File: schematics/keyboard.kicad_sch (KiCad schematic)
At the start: 32 parts, among them J2 Mini-DIN-6, Q1 2N7000, Q2 2N7000, Q3 2N7000, Q4 2N7000, Q5 2N7000, U18 74HC14, U19 74HC04, U21 ATF22V10C-7, U22 74HC280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

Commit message: done wiring
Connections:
- net D5: now also U21.17 (D5), U21.8 (D5IN)
- net D6: now also U21.16 (D6)
- net D7: now also U21.15 (D7)
- net GND: now also U19.5; no longer U19.3
- net at U22.2 (I7), U23.5 (G), U26.2 (QC)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: no longer U21.15 (D7)
- net at U22.1 (I6), U23.6 (H), U26.3 (QD)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: no longer U21.16 (D6)
- net at U22.13 (I5), U25.11 (A), U26.4 (QE)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: no longer U21.17 (D5), U21.8 (D5IN)
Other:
- moved on the sheet: Q5

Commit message: clock improvements
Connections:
- net ϕ0 renamed ϕ0.0
- net ϕ2 renamed ϕ2.0
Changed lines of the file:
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@@
 		)
 	)
-	(global_label "ϕ2"
+	(global_label "ϕ2.0"
 		(shape input)
 		(at 66.04 40.64 180)
@@
 		)
 		(property "Intersheetrefs" "${INTERSHEET_REFS}"
-			(at 60.5148 40.64 0)
+			(at 58.7005 40.64 0)
 			(hide yes)
 			(show_name no)
@@
 		)
 	)
-	(global_label "ϕ0"
+	(global_label "ϕ0.0"
 		(shape input)
 		(at 66.04 38.1 180)
@@
 		)
 		(property "Intersheetrefs" "${INTERSHEET_REFS}"
-			(at 60.5148 38.1 0)
+			(at 58.7005 38.1 0)
 			(hide yes)
 			(show_name no)

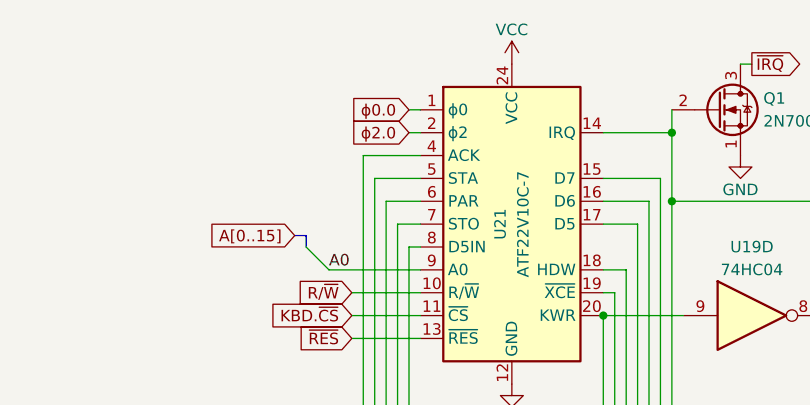
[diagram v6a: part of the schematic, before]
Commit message: ditched phi0, dropped to 6MHz
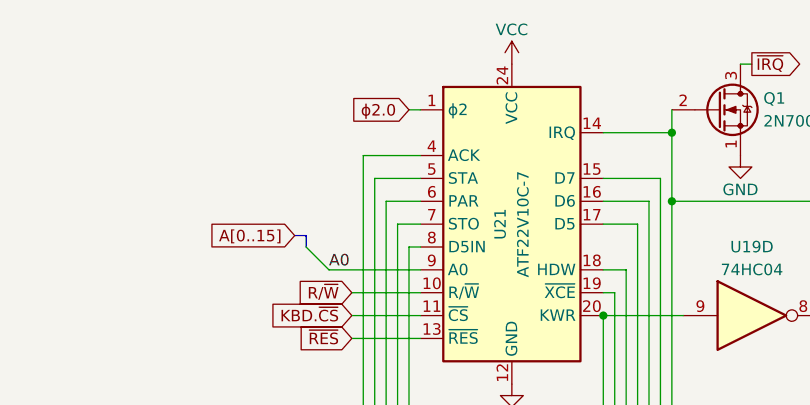
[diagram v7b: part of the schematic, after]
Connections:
- net ϕ0.0 is gone; now on net ϕ2.0: U21.1 (ϕ2)
- net ϕ2.0: no longer U21.2 (ϕ2)
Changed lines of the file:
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@@
-	(wire
-		(pts
-			(xy 66.04 40.64) (xy 67.31 40.64)
-		)
-		(stroke
-			(width 0)
-			(type default)
-		)
-	)
 	(wire
 		(pts
@@
 		)
 	)
-	(global_label "ϕ2.0"
-		(shape input)
-		(at 66.04 40.64 180)
-		(fields_autoplaced yes)
-		(effects
-			(font
-				(size 1.27 1.27)
-			)
-			(justify right)
-		)
-		(property "Intersheetrefs" "${INTERSHEET_REFS}"
-			(at 58.7005 40.64 0)
-			(hide yes)
-			(show_name no)
-			(do_not_autoplace no)
-			(effects
-				(font
-					(size 1.27 1.27)
-				)
-				(justify right)
-			)
-		)
-	)
 	(global_label "KBD.~{CS}"
 		(shape input)
@@
 		)
 	)
-	(global_label "ϕ0.0"
+	(global_label "ϕ2.0"
 		(shape input)
 		(at 66.04 38.1 180)

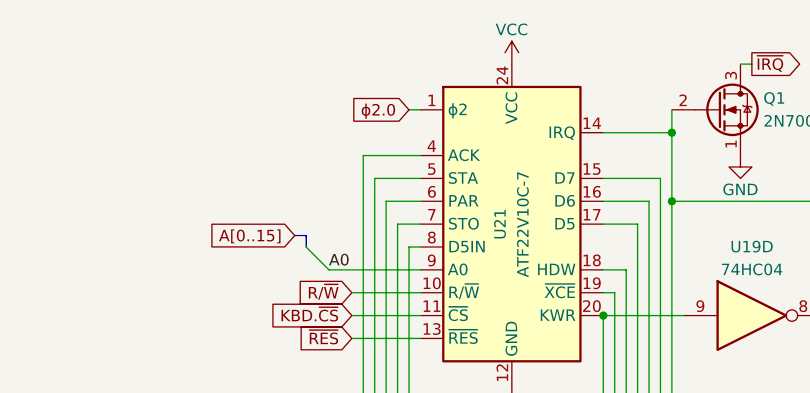
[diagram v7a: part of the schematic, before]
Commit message: keyboard input works
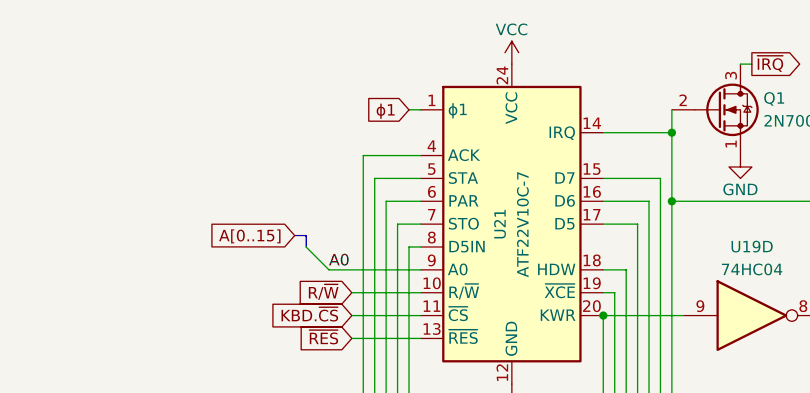
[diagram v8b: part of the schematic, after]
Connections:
- net ϕ2.0 renamed ϕ1
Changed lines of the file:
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@@
 		)
 	)
-	(global_label "ϕ2.0"
+	(global_label "ϕ1"
 		(shape input)
 		(at 66.04 38.1 180)
@@
 		)
 		(property "Intersheetrefs" "${INTERSHEET_REFS}"
-			(at 58.7005 38.1 0)
+			(at 60.5148 38.1 0)
 			(hide yes)
 			(show_name no)
